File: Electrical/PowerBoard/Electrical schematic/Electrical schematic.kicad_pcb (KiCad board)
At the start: 2 copper layers, 21 parts, among them J1 S4B-XH-SM4-TB, J2 XT60PW-M, J3 XT60PW-M, J5 XT60PW-M, U1 LMZ22005TZ/NOPB, U2 ACS715LLCTR-30A-T, U3 TLV2370IDBVR, U4 74LVC1G157GV_125, U5 USB-A-S-RA-TSMT

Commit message: 3rd Iteration PCB
New PCB
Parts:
- removed the REF** at (112.5, 78.0)
- removed the REF** at (112.5, 106.5)
- removed the REF** at (158.0, 106.5)
- added REF**: MountingHole_2.5mm, MountingHole:MountingHole_2.5mm, F.Cu at (161.0, 104.5)
- added REF**: MountingHole_2.5mm, MountingHole:MountingHole_2.5mm, F.Cu at (106.0, 98.5)
- added REF**: MountingHole_2.5mm, MountingHole:MountingHole_2.5mm, F.Cu at (161.0, 135.0)
- moved C11 59.6 mm to (141.5, 133.0), turned to 0 degrees
- moved U2 53.9 mm to (132.8, 131.9), turned to 0 degrees
- moved C10 53.0 mm to (141.5, 130.0), turned to 0 degrees
- moved J3 45.8 mm to (119.2, 114.6), turned to 90 degrees
- moved J2 40.0 mm to (119.2, 134.6)
- moved R4 38.0 mm to (128.4, 108.5), turned to 180 degrees
- moved R3 37.6 mm to (128.4, 112.0)
- moved C3 35.0 mm to (152.0, 130.5)
- moved C2 34.5 mm to (152.0, 122.0)
- moved C1 34.0 mm to (152.0, 113.5)
- moved U4 34.0 mm to (134.5, 104.0)
- moved U3 33.6 mm to (134.5, 110.5), turned to 0 degrees
- moved U1 33.2 mm to (133.4, 120.8)
- moved R2 29.3 mm to (140.1, 113.5), turned to 180 degrees
- moved J5 27.1 mm to (148.9, 96.2)
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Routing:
- net GND: track 181.9 -> 233.0 mm, vias 11 -> 15
- net /Current Sensor/VOLTAGE OUT (of reading): track 9.99 -> 48.4 mm
- net /Buck Converter/Vin (12V): track 58.6 -> 78.4 mm, vias 2 -> 0
- net /Buck Converter/Vout (5V 5A): track 124.6 -> 136.4 mm, vias 5 -> 2
- net Net-(U4-Y): track 15.0 -> 25.7 mm, vias 2 -> 4
- net Net-(U4-S): track 7.57 -> 17.5 mm, vias 0 -> 2
- net Net-(U3-IN-): track 20.0 -> 13.8 mm
- net Net-(U1-FB): track 9.87 -> 15.0 mm, vias 0 -> 2
- net /Current Sensor/CURRENT IN: track 16.9 -> 12.3 mm
- net unconnected-(U1-Pad8): vias 81 -> 100
- added copper zone on B.Cu, net GND

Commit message: final version
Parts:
- removed the REF** at (161.0, 104.5)
- removed the REF** at (106.0, 98.5)
- removed the REF** at (161.0, 135.0)
- added REF**: MountingHole_2.5mm, MountingHole:MountingHole_2.5mm, F.Cu at (97.0, 129.5)
- added REF**: MountingHole_2.5mm, MountingHole:MountingHole_2.5mm, F.Cu at (160.0, 66.5)
- added REF**: MountingHole_2.5mm, MountingHole:MountingHole_2.5mm, F.Cu at (160.0, 129.5)
- added REF**: MountingHole_2.5mm, MountingHole:MountingHole_2.5mm, F.Cu at (96.5, 78.5)
- moved J1 36.0 mm to (101.5, 66.0)
- moved C11 35.9 mm to (121.0, 103.5), turned to 180 degrees
- moved J3 32.5 mm to (151.6, 116.5), turned to 180 degrees
- moved C10 29.7 mm to (121.0, 108.5), turned to 180 degrees
- moved R1 25.1 mm to (142.9, 86.0)
- moved C3 25.1 mm to (153.5, 105.5)
- moved C2 25.0 mm to (153.5, 97.0)
- moved C1 25.0 mm to (153.5, 88.5)
- moved U2 24.9 mm to (131.0, 107.1), turned to 180 degrees
- moved R2 24.6 mm to (142.9, 89.0)
- moved U1 24.1 mm to (135.9, 96.8)
- moved J2 22.1 mm to (131.8, 116.5), turned to 180 degrees
- moved U4 22.0 mm to (117.5, 90.0), turned to 90 degrees
- moved U3 21.5 mm to (117.4, 97.5), turned to 180 degrees
- moved U5 20.4 mm to (126.5, 75.8)
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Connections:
- U1 pad 2: GND -> /Buck Converter/Vin (12V)
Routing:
- net GND: track 233.0 -> 0.00 mm, vias 15 -> 13
- net /Buck Converter/Vout (5V 5A): track 136.4 -> 23.0 mm
- net /Buck Converter/Vin (12V): track 78.4 -> 14.3 mm
- net /Current Sensor/VOLTAGE OUT (of reading): track 48.4 -> 32.7 mm, vias 2 -> 4
- net Net-(U4-S): track 17.5 -> 30.3 mm
- net /Current Sensor/CURRENT IN: track 12.3 -> 0.00 mm
- net Net-(U4-Y): track 25.7 -> 34.1 mm, vias 4 -> 0
- net Net-(U3-IN-): track 13.8 -> 9.33 mm
- net Net-(U2-FILTER): track 4.16 -> 7.12 mm
- net Net-(U3-IN+): track 7.75 -> 9.36 mm
- net Net-(U1-FB): track 15.0 -> 16.1 mm
- added copper zone on F.Cu, net /Buck Converter/Vin (12V)
- added copper zone on F.Cu, net /Buck Converter/Vout (5V 5A)
- added copper zone on F.Cu, net /Current Sensor/CURRENT IN

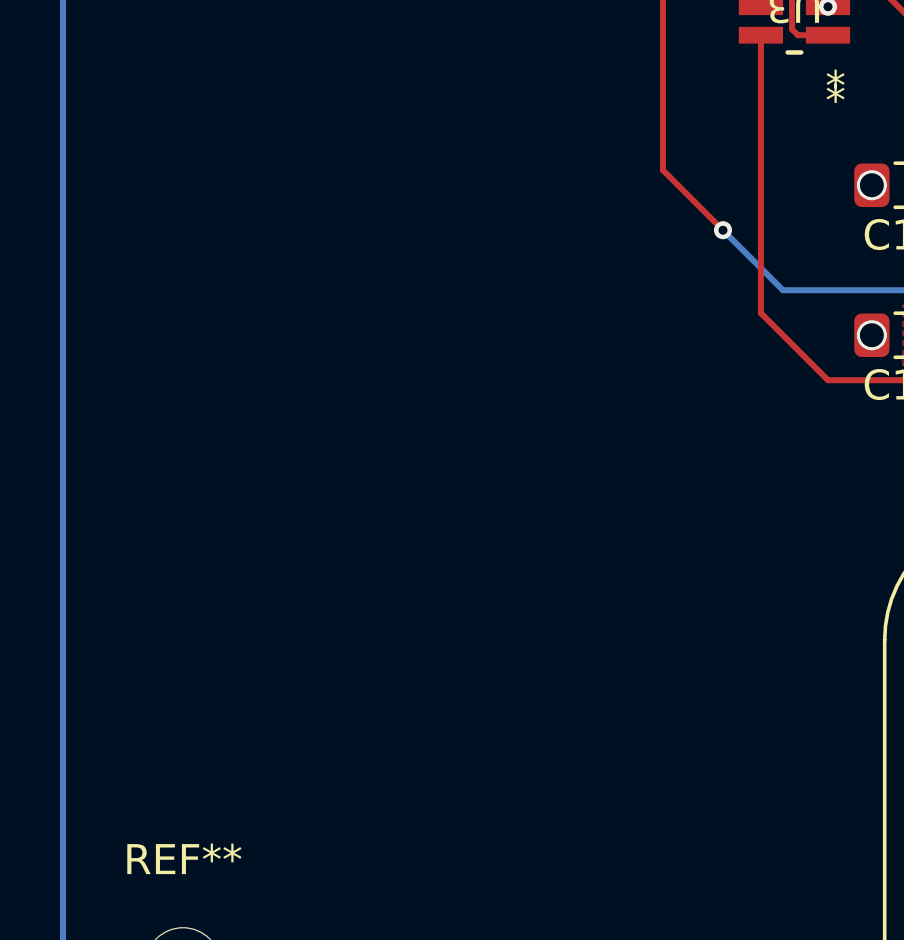
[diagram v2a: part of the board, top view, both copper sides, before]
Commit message: Added dog
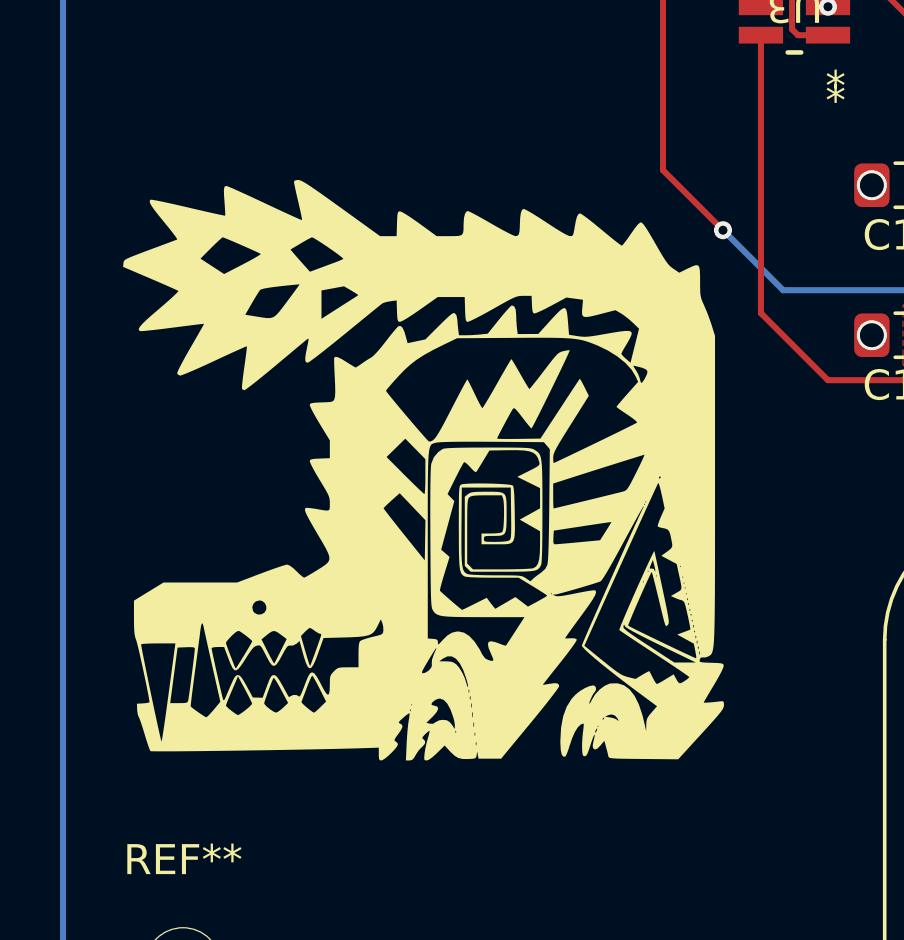
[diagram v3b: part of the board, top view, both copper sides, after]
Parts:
- added G***: LOGO, library:odogaron_l, F.Cu at (105.0, 113.0)
